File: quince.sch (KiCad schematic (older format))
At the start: 116 parts, among them J1 NEIGHBOR1, J10 Conn_01x01, J11 Conn_01x01, J12 Conn_01x01, J13 Conn_01x01, J14 Conn_01x01, J15 Conn_01x01, J16 Conn_01x01, J17 Conn_01x01, J18 Conn_01x01, J19 GND, J2 NEIGHBOR2, J20 Conn_01x01, J21 Conn_01x01, J3 RFIN, J4 Conn_01x01, J5 Conn_01x01, J6 Conn_01x01, J7 BONUS_ROW, J8 LO, J9 Conn_01x01, U1 TLV3502, U2 AD8347, U3 SAW FILTER, U4 LNA, U5 BAND PASS FILTER, U6 ADF4360, X1 TCXO

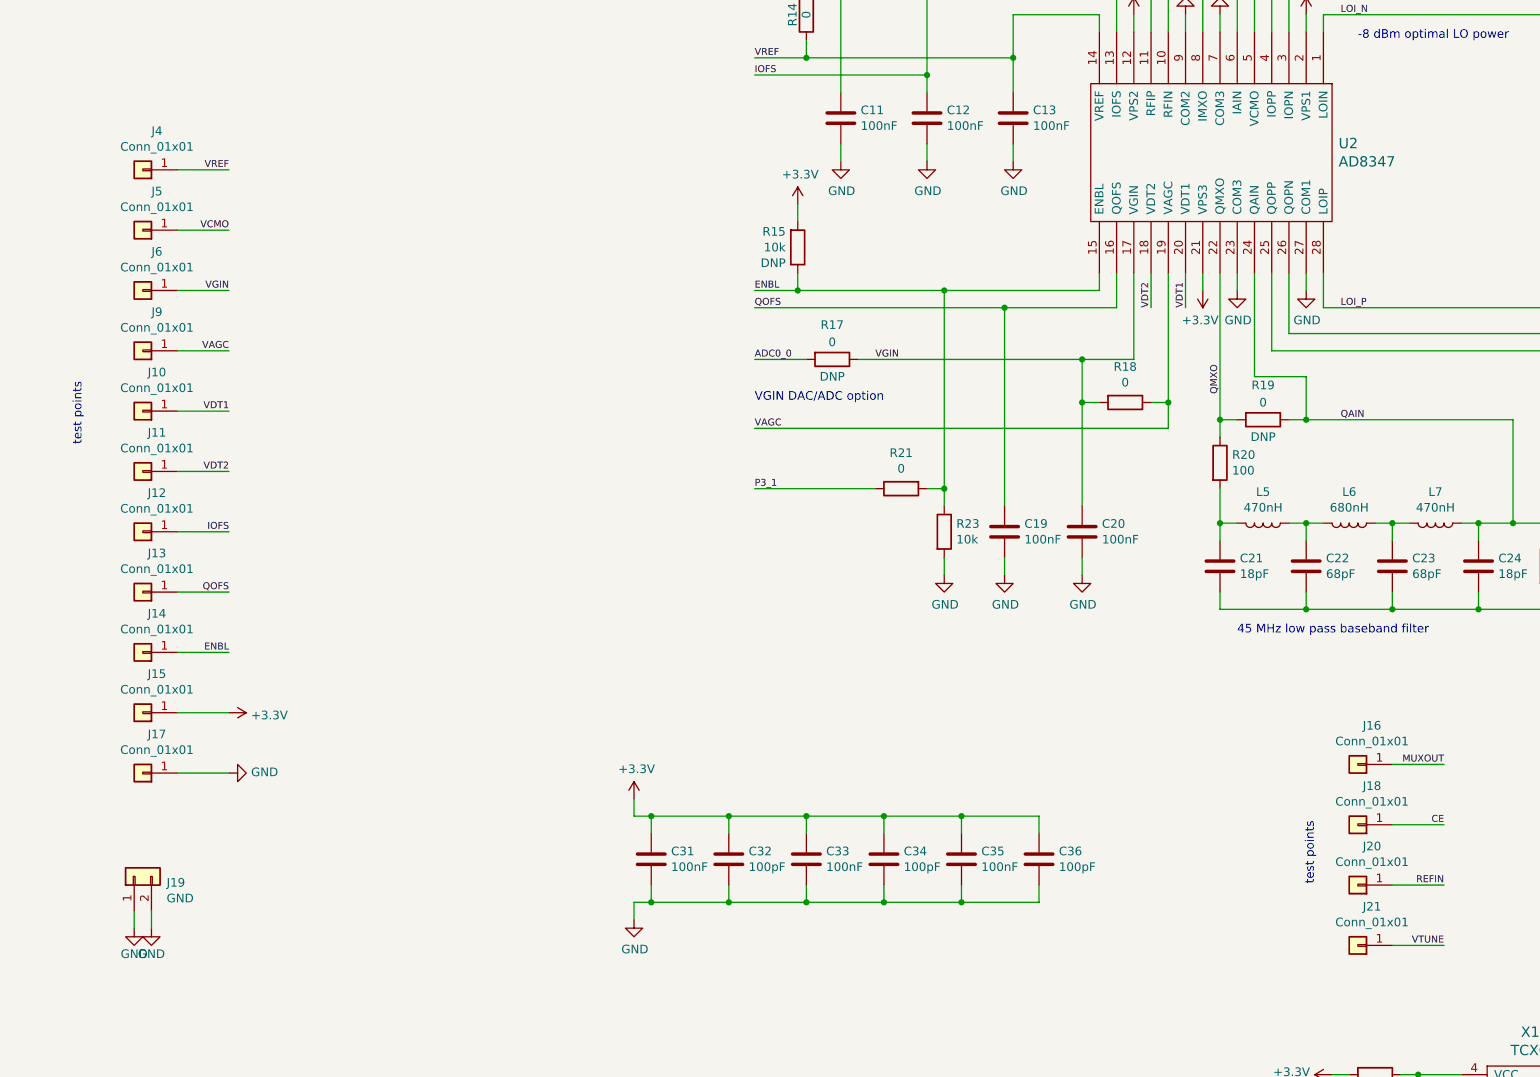
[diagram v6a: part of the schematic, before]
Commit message: use proper test point symbols
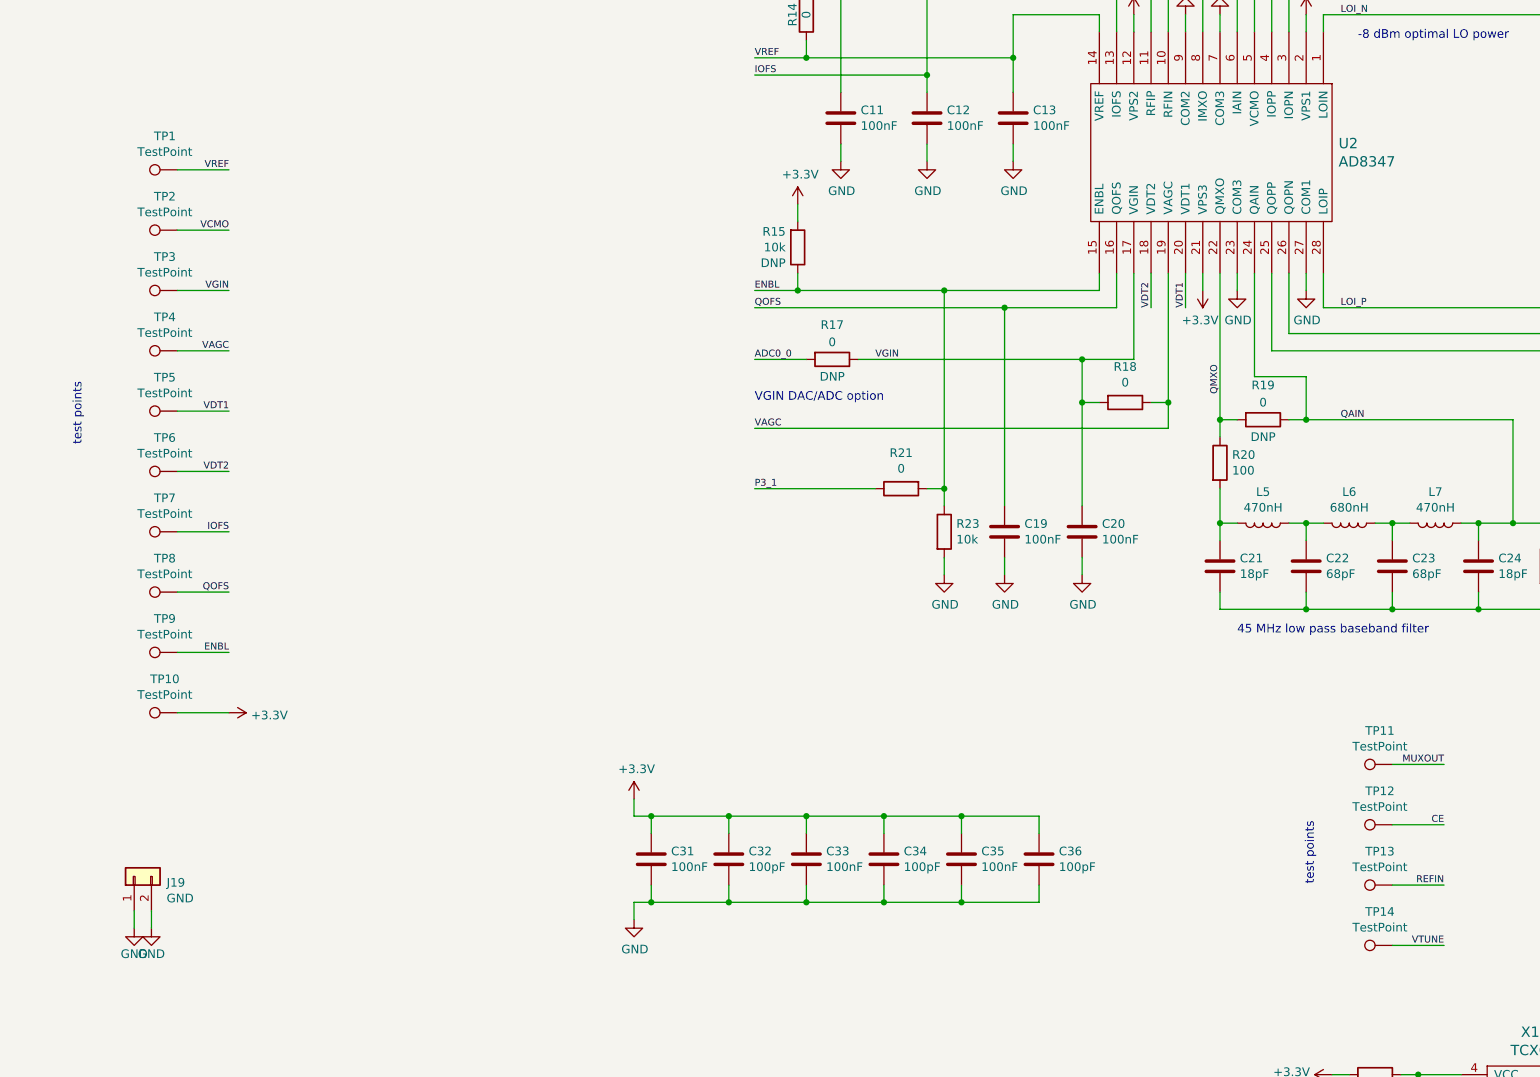
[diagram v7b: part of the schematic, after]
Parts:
- removed J10, J11, J12, J13, J14, J15, J16, J17, J18, J20, J21, J4, J5, J6, J9: Conn_01x01, gsg-modules:TESTPOINT-50MIL, symbol Connector_Generic:Conn_01x01
- added TP1, TP10, TP11, TP12, TP13, TP14, TP2, TP3, TP4, TP5, TP6, TP7, TP8, TP9: TestPoint, gsg-modules:TESTPOINT-50MIL, symbol Connector:TestPoint
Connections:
- net +3V3: now also TP10.1
- net CE: now also TP12.1
- net ENBL: now also TP9.1
- net IOFS: now also TP7.1
- net MUXOUT: now also TP11.1
- net QOFS: now also TP8.1
- net REFIN: now also TP13.1
- net VAGC: now also TP4.1
- net VCMO: now also TP2.1
- net VDT1: now also TP5.1
- net VDT2: now also TP6.1
- net VGIN: now also TP3.1
- net VREF: now also TP1.1
- net VTUNE: now also TP14.1

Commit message: select parts
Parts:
- C1, C11, C12, C13, C19, C20, C25, C27, C30, C31, C33, C35, C41: Description (none) -> CAP CER 0.1UF 10V X5R 0402; Manufacturer (none) -> Samsung; Part Number (none) -> CL05A104MP5NNNC
- C10, C14, C15, C16, C17, C32, C34, C36, C8, C9: Description (none) -> CAP CER 100PF 50V C0G/NP0 0402; Manufacturer (none) -> Samsung; Part Number (none) -> CL05C101JB5NNNC
- C18: Description (none) -> CAP CER 270PF 50V X7R 0402; Manufacturer (none) -> Samsung; Part Number (none) -> CL05B271KB5NNNC
- C2, C39, C40, C7: Description (none) -> CAP CER 1000PF 50V X7R 0402; Manufacturer (none) -> Taiyo Yuden; Part Number (none) -> UMK105B7102KV-F
- C21, C24, C3, C6: Description (none) -> CAP CER 18PF 50V C0G/NPO 0402; Manufacturer (none) -> Yageo; Part Number (none) -> CC0402JRNPO9BN180
- C22, C23, C4, C5: Description (none) -> CAP CER 68PF 50V C0G/NP0 0402; Manufacturer (none) -> Samsung; Part Number (none) -> CL05C680JB5NNNC
- C26: Description (none) -> CAP CER 8200PF 16V X7R 0402; Manufacturer (none) -> Yageo; Part Number (none) -> CC0402KRX7R7BB822
- C28: Description (none) -> CAP CER 560PF 50V X7R 0402; Manufacturer (none) -> Samsung; Part Number (none) -> CL05B561KB5NNNC
- C29: Description (none) -> CAP CER 10000PF 50V X7R 0402; Manufacturer (none) -> Samsung; Part Number (none) -> CL05B103KB5NNNC
- C37: Description (none) -> CAP CER 10UF 10V X5R 0805; Manufacturer (none) -> Samsung; Part Number (none) -> CL21A106KPFNNNG
- D1: Description (none) -> TVS DIODE 4V 1005; Manufacturer (none) -> Murata; Part Number (none) -> LXES15AAA1-153
- FB1: Description (none) -> FERRITE BEAD 220 OHM 0805 1LN; Manufacturer (none) -> Murata; Part Number (none) -> BLM21PG221SN1D
- J19, TP1, TP10, TP11, TP12, TP13, TP14, TP2, TP3, TP4, TP5, TP6, TP7, TP8, TP9: Note (none) -> DNP
- J3: Description (none) -> CONN RPSMA RCPT STR 50OHM EDGEMT; Manufacturer (none) -> Linx Technologies; Part Number (none) -> CONREVSMA003.062
- J8: Description (none) -> CONN SMA JACK STR 50 OHM PCB; Manufacturer (none) -> TE Connectivity; Part Number (none) -> 5-1814832-1
- L1, L3, L5, L7: Description (none) -> FIXED IND 470NH 20MA 420 MOHM; Manufacturer (none) -> Taiyo Yuden; Part Number (none) -> LK1005R47K-TV
- L2, L6: Description (none) -> FIXED IND 680NH 20MA 550 MOHM; Manufacturer (none) -> Taiyo Yuden; Part Number (none) -> LK1005R68K-TV
- L4: Description (none) -> FIXED IND 3.6NH 500MA 200 MOHM; Manufacturer (none) -> Tayo Yuden; Part Number (none) -> HK10053N6S-T
- R1, R12, R13, R14, R17, R18, R19, R2, R21, R3, R30, R32, R4, R5, R6: Description (none) -> RES SMD 0 OHM JUMPER 1/16W 0402; Manufacturer (none) -> Yageo; Part Number (none) -> RC0402JR-070RL
- R10, R16: Description (none) -> RES SMD 200 OHM 5% 1/16W 0402; Manufacturer (none) -> Yageo; Part Number (none) -> RC0402JR-07200RL
- R11, R20, R25, R7: Description (none) -> RES SMD 100 OHM 5% 1/16W 0402; Manufacturer (none) -> Yageo; Part Number (none) -> RC0402JR-07100RL
- R15, R23: Description (none) -> RES SMD 10K OHM 5% 1/16W 0402; Manufacturer (none) -> Yageo; Part Number (none) -> RC0402JR-0710KL
- R22, R9: Description (none) -> RES SMD 2.2K OHM 5% 1/16W 0402; Manufacturer (none) -> Yageo; Part Number (none) -> RC0402JR-072K2L
- R24, R28, R33: Description (none) -> RES SMD 51 OHM 5% 1/16W 0402; Manufacturer (none) -> Yageo; Part Number (none) -> RC0402JR-0751RL
- R26, R31, R8: Description (none) -> RES SMD 3.3K OHM 5% 1/16W 0402; Manufacturer (none) -> Yageo; Part Number (none) -> RC0402JR-073K3L
- R27: Description (none) -> RES SMD 3K OHM 5% 1/16W 0402; Manufacturer (none) -> Yageo; Part Number (none) -> RC0402JR-073KL
- R29: Description (none) -> RES SMD 1.5K OHM 5% 1/16W 0402; Manufacturer (none) -> Yageo; Part Number (none) -> RC0402JR-071K5L
